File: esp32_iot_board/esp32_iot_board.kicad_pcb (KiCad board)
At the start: 2 copper layers, 100 x 100 mm, 62 parts, among them J1 USB_C_Receptacle_USB2.0, J2 Conn_01x04, J3 Screw_Terminal_01x03, J4 Screw_Terminal_01x08, J5 Screw_Terminal_01x02, J6 Conn_02x05_Odd_Even, K1 RT314A05, Q1 UMH3N, Q2 BC817, SW1 SW_SPST, U1 ESP32-WROOM-32D, U2 USBLC6-2P6, U3 CP2104, U4 Si7020-A20, U5 74AHCT245, U6 TLV1117LV-3.3

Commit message: 2.06h
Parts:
- moved C7 160.5 mm to (105.9, 97.2), turned to -90 degrees
- moved C9 155.1 mm to (116.6, 67.0), turned to 90 degrees
- moved R1 154.9 mm to (98.9, 94.9), turned to -90 degrees
- moved C14 154.7 mm to (123.7, 63.5)
- moved C15 154.7 mm to (123.7, 66.8)
- moved R2 151.8 mm to (101.3, 94.9), turned to -90 degrees
- moved C8 145.1 mm to (121.7, 93.1)
- moved R10 141.0 mm to (120.3, 113.1)
- moved R8 141.0 mm to (120.3, 106.6)
- moved R9 141.0 mm to (120.3, 109.8)
- moved R7 138.9 mm to (116.6, 72.6), turned to 90 degrees
- moved R6 138.5 mm to (119.8, 87.9), turned to 90 degrees
- moved R11 137.2 mm to (123.4, 58.7)
- moved R17 95.7 mm to (171.6, 76.2)
- moved R18 95.7 mm to (171.6, 79.5)
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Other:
- outline, holes or cut-outs redrawn

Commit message: prog routed
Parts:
- removed C1: 1000u/25V, Capacitor_THT:C_Radial_D10.0mm_H12.5mm_P5.00mm
- removed C11: 22u, Capacitor_SMD:C_1206_3216Metric
- removed C12, C13: 100nf, Capacitor_SMD:C_1206_3216Metric
- removed D1: LL4148, Diode_SMD:D_MiniMELF
- removed D2: YELLOW, LED_SMD:LED_1206_3216Metric
- removed F1: Fuse, Fuse:Fuse_1206_3216Metric_Pad1.42x1.75mm_HandSolder
- removed J3: Screw_Terminal_01x03, TerminalBlock_Phoenix:TerminalBlock_Phoenix_PT-1,5-3-5.0-H_1x03_P5.00mm_Horizontal
- removed J4: Screw_Terminal_01x08, TerminalBlock_Phoenix:TerminalBlock_Phoenix_PT-1,5-8-5.0-H_1x08_P5.00mm_Horizontal
- removed J5: Screw_Terminal_01x02, TerminalBlock_Phoenix:TerminalBlock_Phoenix_MKDS-3-3-5.08_1x03_P5.08mm_Horizontal
- removed K1: RT314A05, Relay_THT:Relay_SPDT_Schrack-RT1-16A-FormC_RM5mm
- removed Q2: BC817, Package_TO_SOT_SMD:SOT-23
- removed R12, R13: 4k7, Resistor_SMD:R_1206_3216Metric
- removed R14: 10k, Resistor_SMD:R_1206_3216Metric
- removed R15, R16: 1k, Resistor_SMD:R_1206_3216Metric
- removed R17, R18, R19, R20: 22R, Resistor_SMD:R_1206_3216Metric
- removed U4: Si7020-A20, Package_DFN_QFN:DFN-6-1EP_3x3mm_P1mm_EP1.5x2.4mm
- removed U5: 74AHCT245, Package_DIP:DIP-20_W7.62mm
- J2: value Conn_01x04 -> Screw_Terminal_01x02; footprint Connector_JST:JST_SH_SM04B-SRSS-TB_1x04-1MP_P1.00mm_Horizontal -> TerminalBlock_Phoenix:TerminalBlock_Phoenix_PT-1,5-2-5.0-H_1x02_P5.00mm_Horizontal
- moved C6 158.3 mm to (104.1, 90.8), turned to -90 degrees
- moved C5 155.4 mm to (106.5, 90.8), turned to -90 degrees
- moved C10 152.9 mm to (123.5, 56.3), turned to 180 degrees
- moved C3 152.3 mm to (109.0, 90.8), turned to -90 degrees
- moved C4 145.6 mm to (115.5, 96.1), turned to -90 degrees
- moved C2 142.9 mm to (117.9, 96.1), turned to -90 degrees
- moved R3 134.1 mm to (117.0, 86.0), turned to -90 degrees
- moved D3 63.4 mm to (167.4, 78.8), turned to 90 degrees
- moved SW1 61.1 mm to (168.1, 69.8), turned to 180 degrees
- moved R9 52.0 mm to (160.2, 76.4)
- moved R10 50.5 mm to (160.2, 82.2)
- moved R8 48.3 mm to (160.2, 79.3)
- moved C9 43.8 mm to (160.4, 65.6)
- moved R7 41.7 mm to (158.1, 68.6)
- moved D4 16.8 mm to (125.4, 98.6), turned to 0 degrees
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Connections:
- J2 pad 2: +3V3 -> +5VP
- U2 pad 1: Net-(J1-D--PadA7) -> Net-(J1-D+-PadA6)
- U2 pad 3: Net-(J1-D+-PadA6) -> Net-(J1-D--PadA7)
- U2 pad 4: Net-(U3-D+) -> Net-(U3-D-)
- U2 pad 5: unconnected-(U2-VBUS-Pad5) -> +5V
- U2 pad 6: Net-(U3-D-) -> Net-(U3-D+)
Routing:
- net Net-(U3-RXD): track 0.00 -> 70.0 mm, vias 0 -> 2
- net Net-(U3-TXD): track 0.00 -> 60.4 mm, vias 0 -> 2
- net +5VP: track 0.00 -> 48.7 mm
- net /IO0: track 0.00 -> 46.6 mm, vias 0 -> 2
- net +5V: track 0.00 -> 36.0 mm
- net /LED_B: track 0.00 -> 33.4 mm
- net +3.3VA: track 0.00 -> 31.1 mm, vias 0 -> 2
- net /EN: track 0.00 -> 30.2 mm
- net /LED_R: track 0.00 -> 25.9 mm
- net /SW: track 0.00 -> 17.6 mm
- net /LED_G: track 0.00 -> 15.7 mm
- net /DTR: track 0.00 -> 13.8 mm
- net Net-(J1-CC2): track 0.00 -> 10.1 mm, vias 0 -> 2
- net /RTS: track 0.00 -> 9.36 mm
- net Net-(D3-GK): track 0.00 -> 8.86 mm
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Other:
- copper layers 2 -> 4
- board text added: "+5V"
- board text added: "gnd"

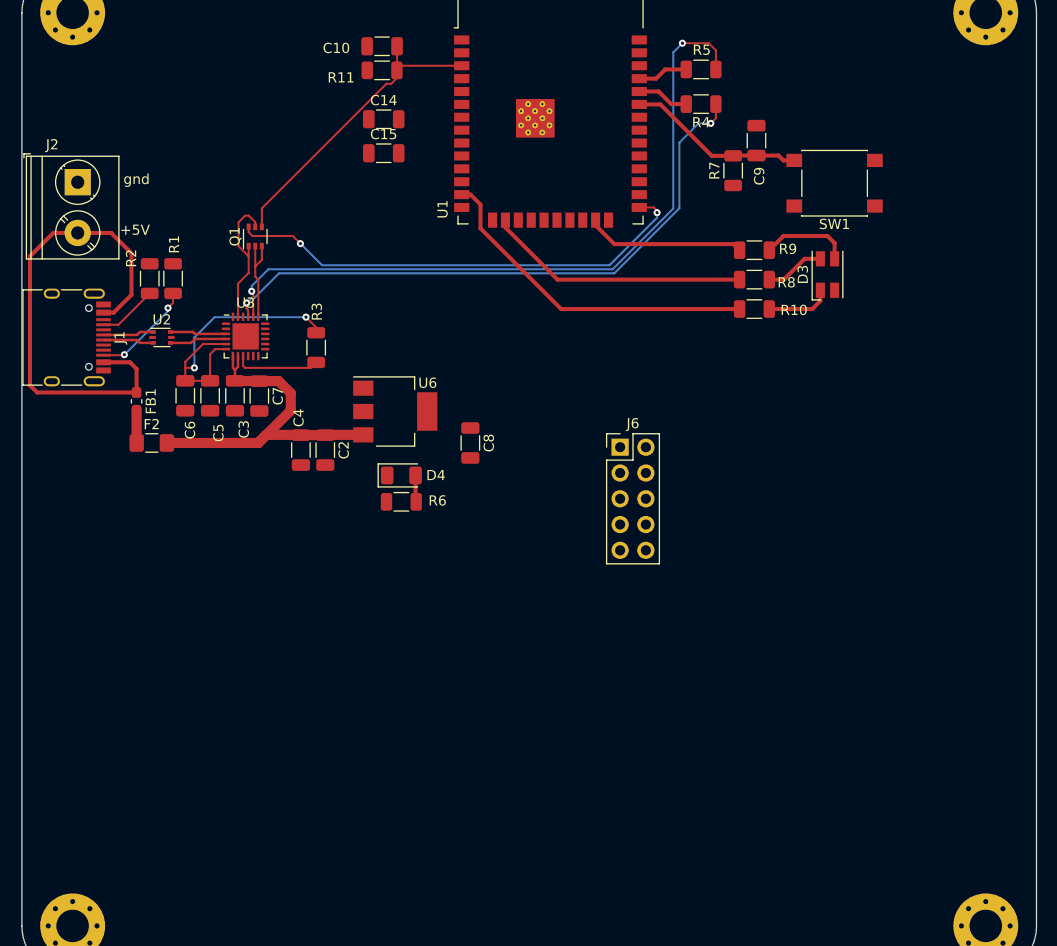
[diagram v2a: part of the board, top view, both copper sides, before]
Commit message: added i2c and onewire
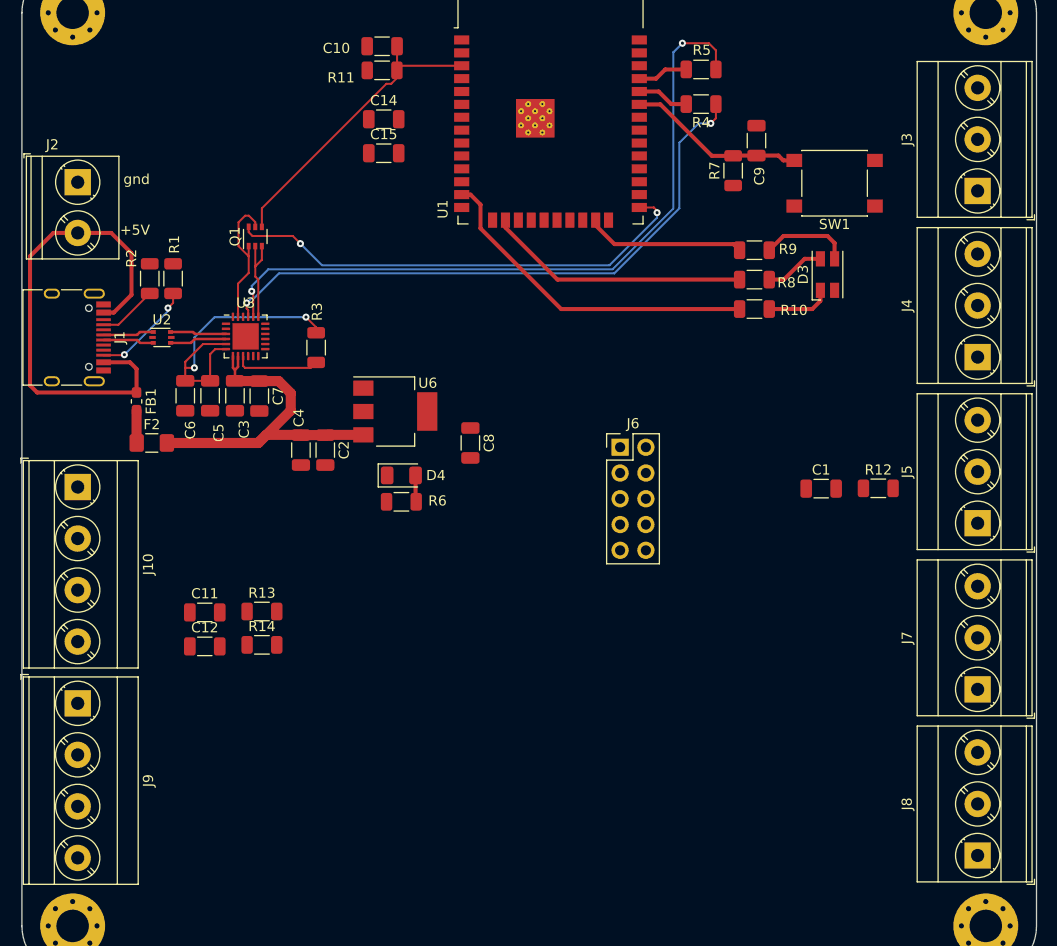
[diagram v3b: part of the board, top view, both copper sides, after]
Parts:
- added C1: 100nf, Capacitor_SMD:C_1206_3216Metric, F.Cu at (166.8, 99.9)
- added C11: 100nf, Capacitor_SMD:C_1206_3216Metric, F.Cu at (106.0, 112.1)
- added C12: 100nf, Capacitor_SMD:C_1206_3216Metric, F.Cu at (106.0, 115.5)
- added J10: Screw_Terminal_01x04, TerminalBlock_Phoenix:TerminalBlock_Phoenix_MKDS-3-4-5.08_1x04_P5.08mm_Horizontal, F.Cu at (93.5, 99.7)
- added J3: Screw_Terminal_01x03, TerminalBlock_Phoenix:TerminalBlock_Phoenix_MKDS-3-3-5.08_1x03_P5.08mm_Horizontal, F.Cu at (182.2, 70.6)
- added J4: Screw_Terminal_01x03, TerminalBlock_Phoenix:TerminalBlock_Phoenix_MKDS-3-3-5.08_1x03_P5.08mm_Horizontal, F.Cu at (182.2, 86.9)
- added J5: Screw_Terminal_01x03, TerminalBlock_Phoenix:TerminalBlock_Phoenix_MKDS-3-3-5.08_1x03_P5.08mm_Horizontal, F.Cu at (182.2, 103.3)
- added J7: Screw_Terminal_01x03, TerminalBlock_Phoenix:TerminalBlock_Phoenix_MKDS-3-3-5.08_1x03_P5.08mm_Horizontal, F.Cu at (182.2, 119.7)
- added J8: Screw_Terminal_01x03, TerminalBlock_Phoenix:TerminalBlock_Phoenix_MKDS-3-3-5.08_1x03_P5.08mm_Horizontal, F.Cu at (182.2, 136.1)
- added J9: Screw_Terminal_01x04, TerminalBlock_Phoenix:TerminalBlock_Phoenix_MKDS-3-4-5.08_1x04_P5.08mm_Horizontal, F.Cu at (93.5, 121.1)
- added R12: 4k7, Resistor_SMD:R_1206_3216Metric, F.Cu at (172.4, 99.9)
- added R13: 4k7, Resistor_SMD:R_1206_3216Metric, F.Cu at (111.7, 112.0)
- added R14: 4k7, Resistor_SMD:R_1206_3216Metric, F.Cu at (111.7, 115.3)
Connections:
- U1 pad 27: /LEDSTR1 -> /onewire
- U1 pad 28: /LEDSTR2 -> unconnected-(U1-IO17-Pad28)
- U1 pad 30: /LEDSTR3 -> unconnected-(U1-IO18-Pad30)
